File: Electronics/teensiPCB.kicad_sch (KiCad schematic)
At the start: 15 parts, among them J1 screw terminal, J2 Conn_01x02, J5 UART1, J6 UART2, J7 I2C ext, SW1 SW_Push, U2 SAM-M10Q-00B

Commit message: Updated TODOs
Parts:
- removed J6: UART2, Connector_JST:JST_XH_B4B-XH-A_1x04_P2.50mm_Vertical, symbol Connector_Generic:Conn_01x04
- removed J7: I2C ext, Connector_JST:JST_XH_B4B-XH-A_1x04_P2.50mm_Vertical, symbol Connector_Generic:Conn_01x04
- added UART3: Conn_01x02, Connector_JST:JST_XH_B2B-XH-A_1x02_P2.50mm_Vertical, symbol Connector_Generic:Conn_01x02
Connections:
- net SCL_OUT_MOTOR2: now reaches Ue1.16 (SCL2)
- net SDA_OUT_MOTOR2: now reaches Ue1.17 (SDA2)
- net RX_OUT_MOTOR1: now reaches Ue1.9 (RX2)
- net TX_OUT_MOTOR1: now reaches Ue1.10 (TX2)
- net TX_TO_GCS: now reaches Ue1.42 (TX5)
- net TX_TO_GCS: now also UART3.2 (Pin_2)
- net RX_TO_GCS: now reaches Ue1.43 (RX5)
- net RX_TO_GCS: now also UART3.1 (Pin_1)
- no-connect marks 40 -> 38
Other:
- note added: "Decoupling Caps"
- note added: "GPS I2C Address: 0x42"
- note added: "Output to motors *** Research if we can use both DM556 motor drivers on I2C,"
- note added: "SCREW -> BATTERY Add switch for powering on teensy, from switch out to buck converter"
- note added: "TODO: find buck converter + level converters to put on board identify trace sizes for power lines and add ground net Screw terminal line to buck converter to button/switch for microcontroller power Add buck converter for 24V -> 5V step down Add 5V line for Pulse (+) and Dir (+) pins for each motor driver (total of four power lines going directly from a buck converter) 3.3 -> 5V level converter fo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"
- note added: "UART Breakout"
- note added: "UART to Ground Control Station"
- note removed: "3V3 SDA SCL GND"
- note removed: "I2C Address: 0x42"
- moved on the sheet: C1, C2, H1, H2, J1, J2, R1, R2, R3, SW1, U2

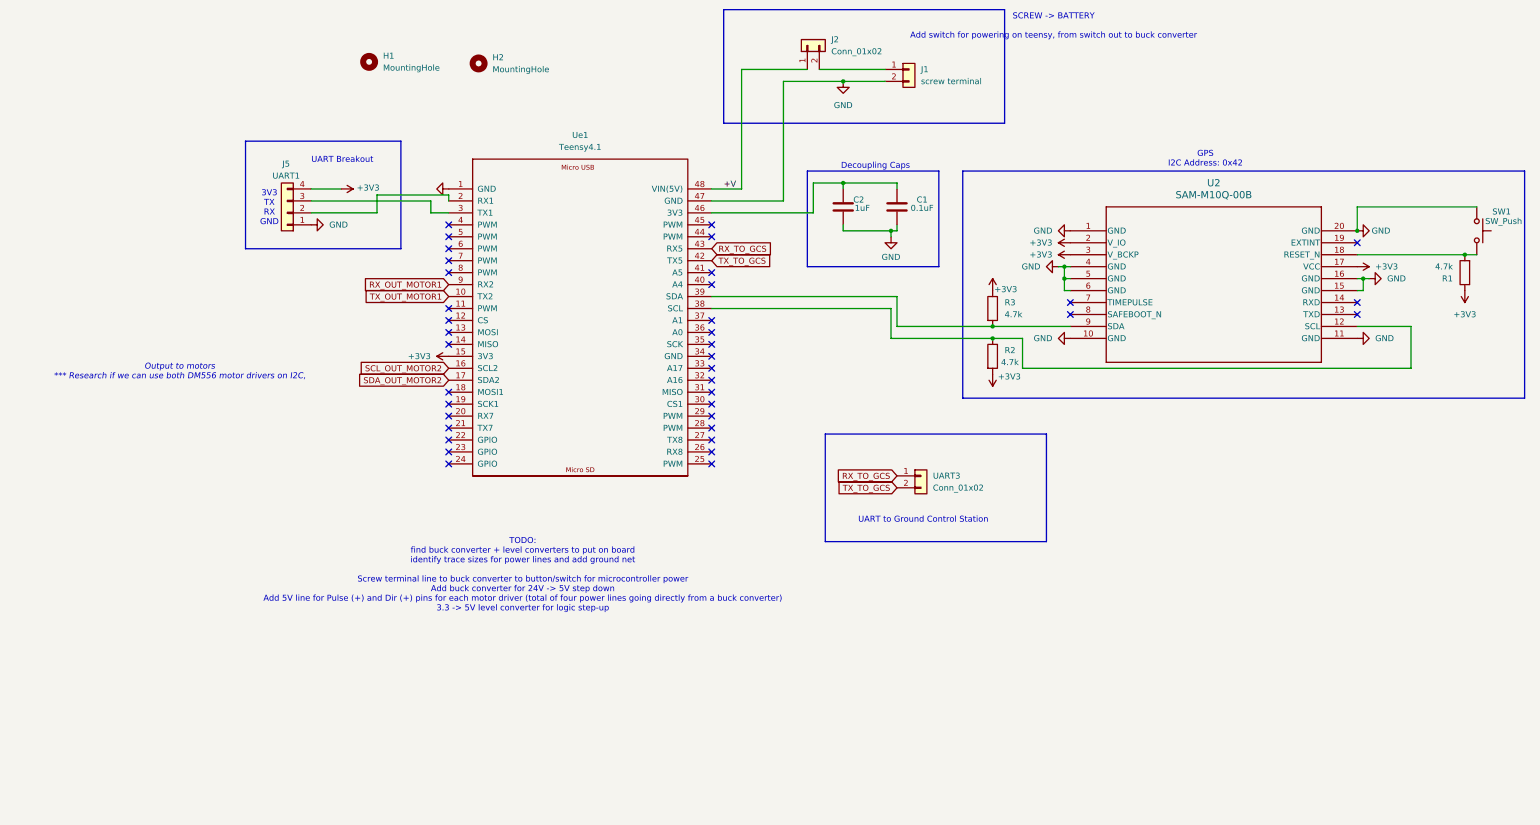
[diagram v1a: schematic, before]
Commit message: Change teensy symbol and footprint
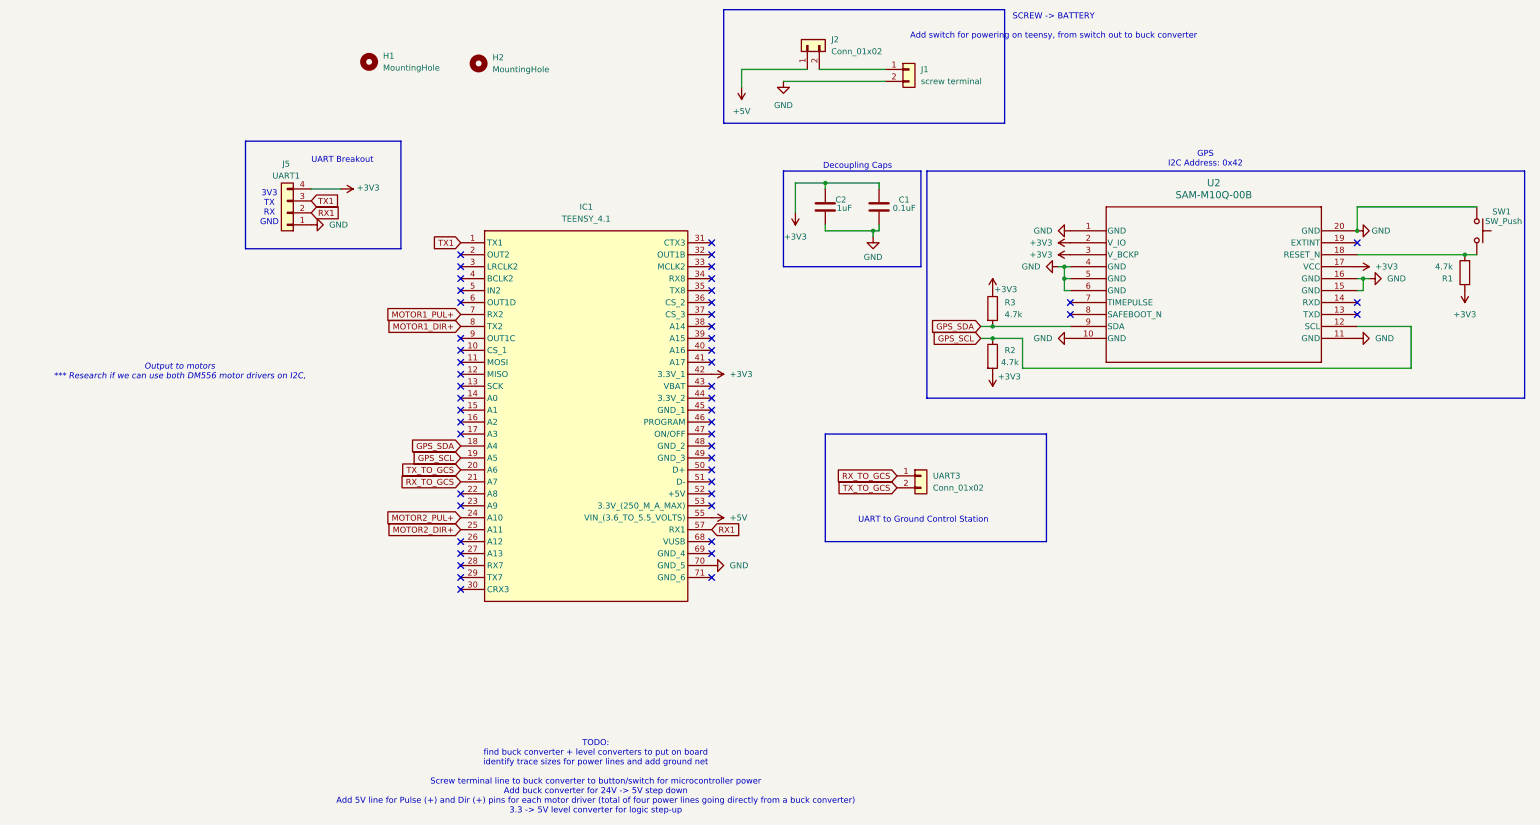
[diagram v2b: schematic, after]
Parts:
- removed Ue1: Teensy4.1, teensy:teensy, symbol teensy:Teensy4.1
- added IC1: TEENSY_4.1, TEENSY41, symbol TEENSY_4_1:TEENSY_4.1
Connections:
- net +3V3: now also C1.1, C2.1, IC1.42 (3.3V_1)
- net GND: now also IC1.70 (GND_5)
- net RX_TO_GCS: now also IC1.21 (A7)
- net TX_TO_GCS: now also IC1.20 (A6)
- net GPS_SCL: now reaches R2.1, U2.12 (SCL)
- net GPS_SCL: now also IC1.19 (A5)
- net RX1: now reaches J5.2 (Pin_2)
- net RX1: now also IC1.57 (RX1)
- net TX1: now reaches J5.3 (Pin_3)
- net TX1: now also IC1.1 (TX1)
- net GPS_SDA: now reaches R3.2, U2.9 (SDA)
- net GPS_SDA: now also IC1.18 (A4)
- net +V renamed +5V
- net +5V: now also IC1.55 (VIN_(3.6_TO_5.5_VOLTS))
- new net MOTOR1_DIR+: IC1.8 (TX2)
- new net MOTOR1_PUL+: IC1.7 (RX2)
- new net MOTOR2_DIR+: IC1.25 (A11)
- new net MOTOR2_PUL+: IC1.24 (A10)
- no-connect marks 38 -> 51
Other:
- moved on the sheet: C1, C2
